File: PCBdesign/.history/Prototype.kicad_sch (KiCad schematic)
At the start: 15 parts, among them J1 AudioJack2, J2 Adafruit Micro-Lipo, SW2 SW_Nidec_CAS-120A1, U1 ESP32-S3-WROOM-2, U2 ER_OLEDM0.91_1x-I2C, U3 AP2112K-3.3, U4 MAX98357A, U5 PCM5102A

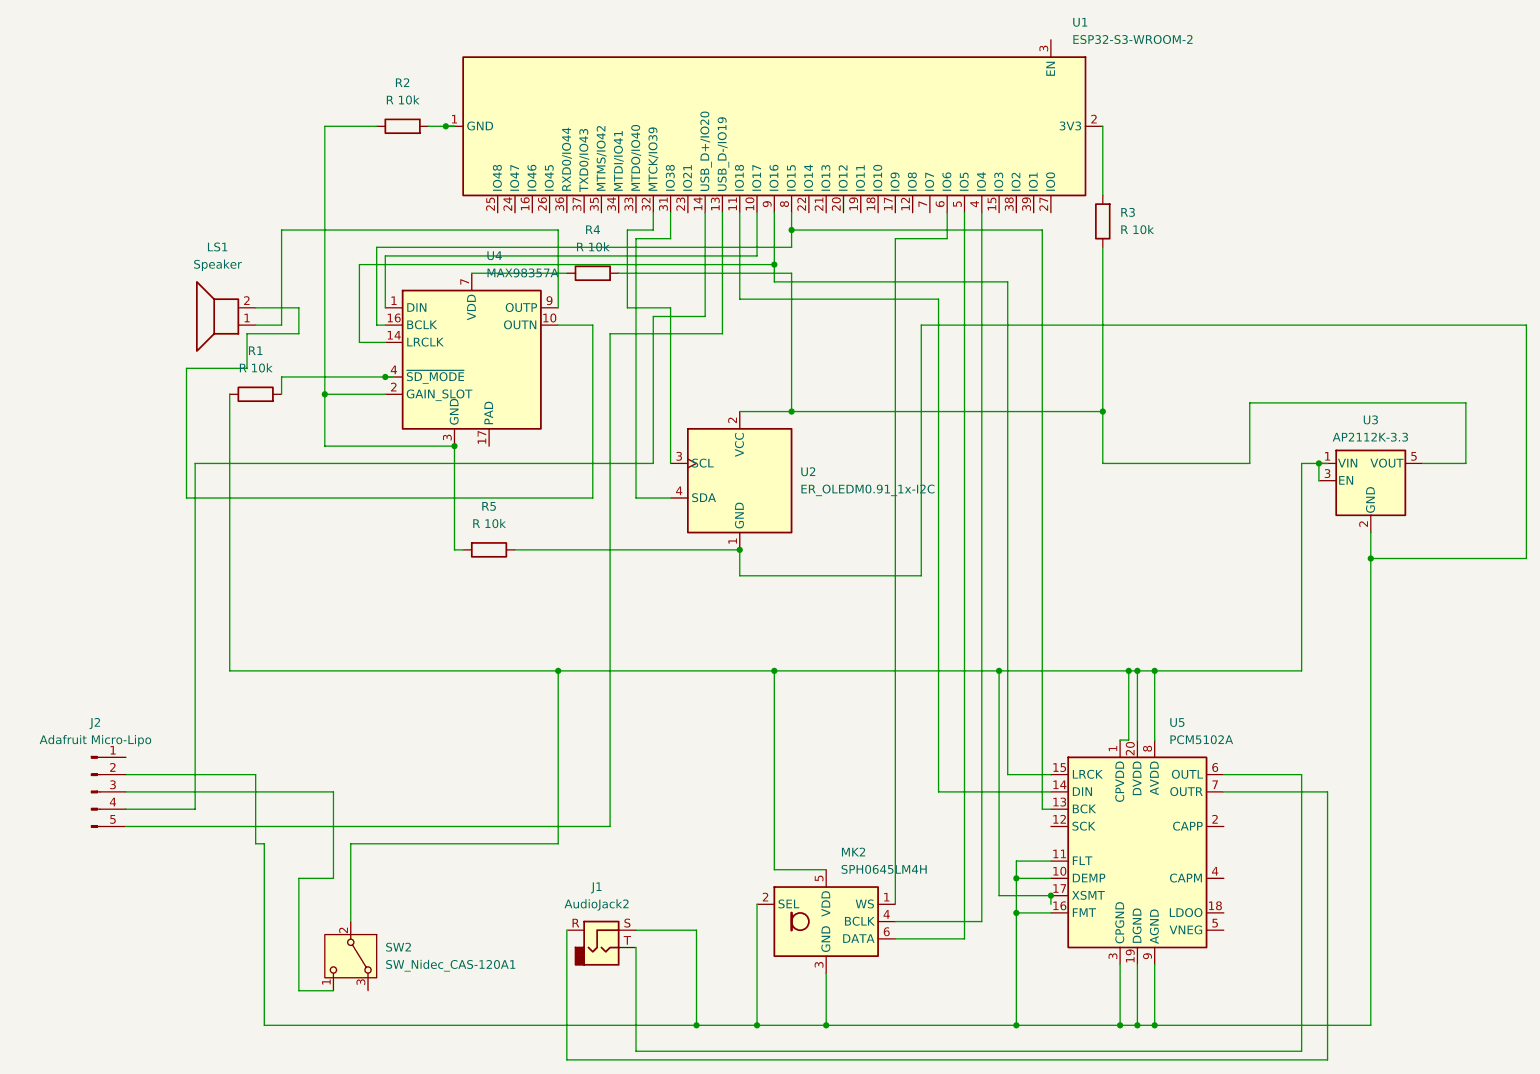
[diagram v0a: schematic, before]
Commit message: Update PCB layout and schematic fixes
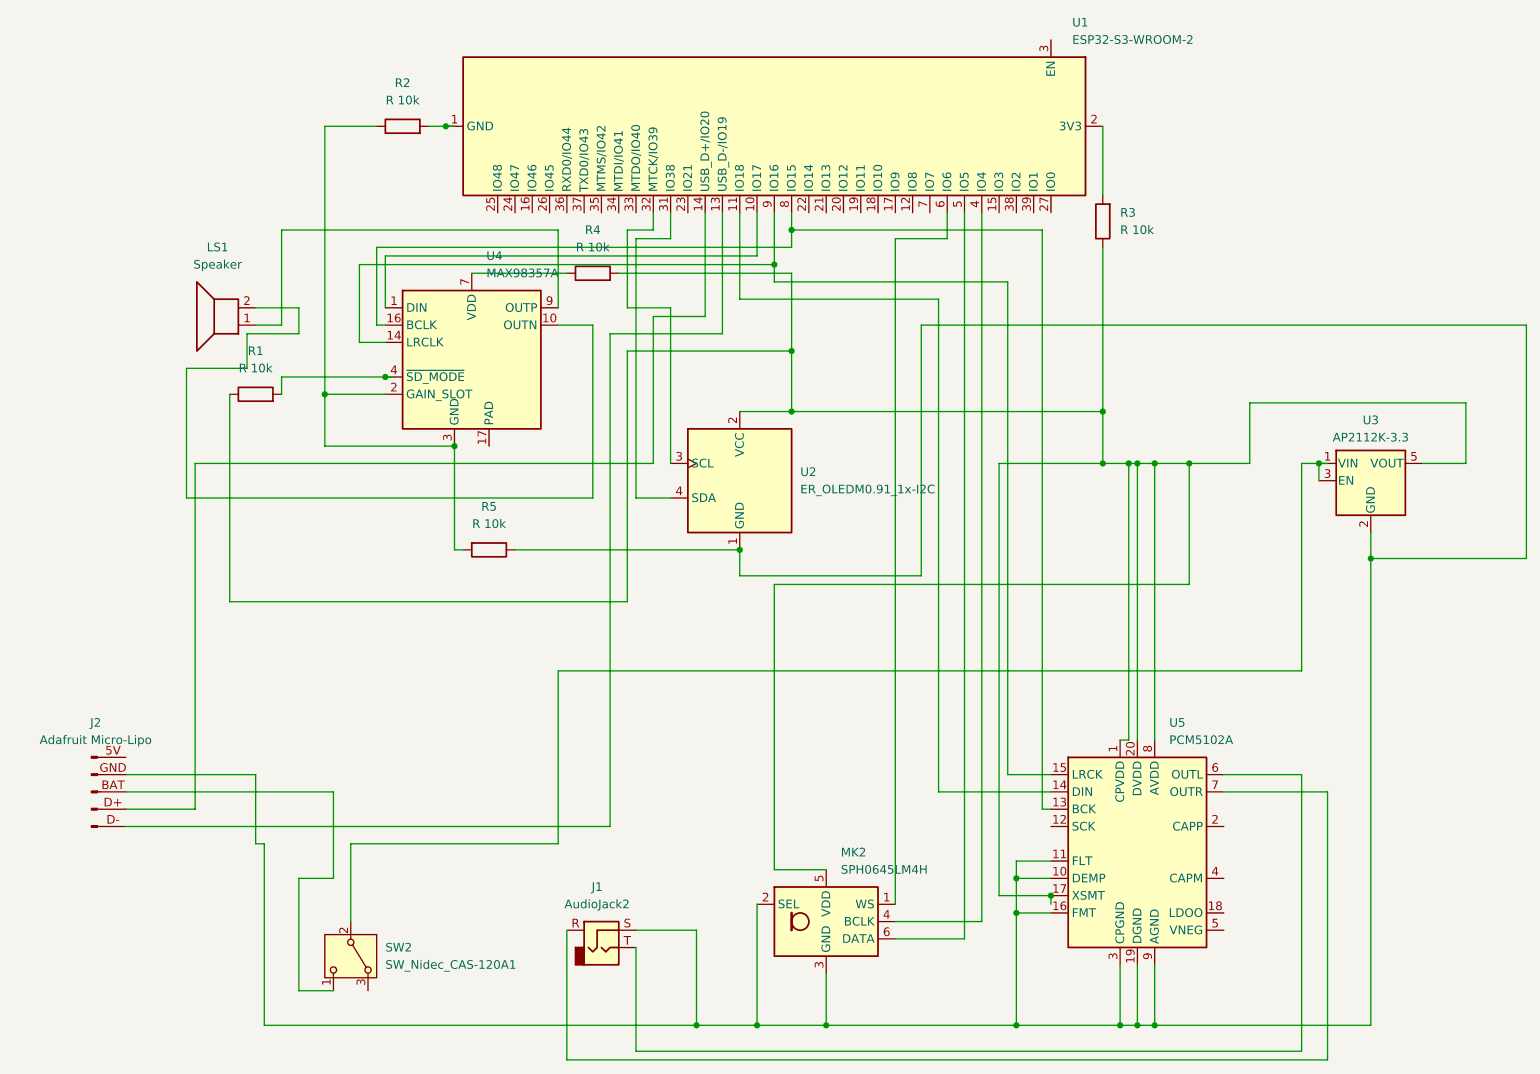
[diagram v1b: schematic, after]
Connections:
- net at R3.1, R4.2, U2.2 (VCC)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: now also MK2.5 (VDD), R1.1, U5.1 (CPVDD), U5.17 (XSMT), U5.20 (DVDD), U5.8 (AVDD)
- net at J1.S, MK2.2 (SEL), MK2.3 (GND)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: now also J2.GND; no longer J2.2 (GND)
- net at SW2.1 (C): now also J2.BAT; no longer J2.3 (BAT)
- net at U1.13 (USB_D-/IO19): now also J2.D-; no longer J2.5 (D-)
- net at U1.14 (USB_D+/IO20): now also J2.D+; no longer J2.4 (D+)
- new net: SW2.2 (B), U3.1 (VIN), U3.3 (EN)
